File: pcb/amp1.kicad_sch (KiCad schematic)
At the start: 23 parts

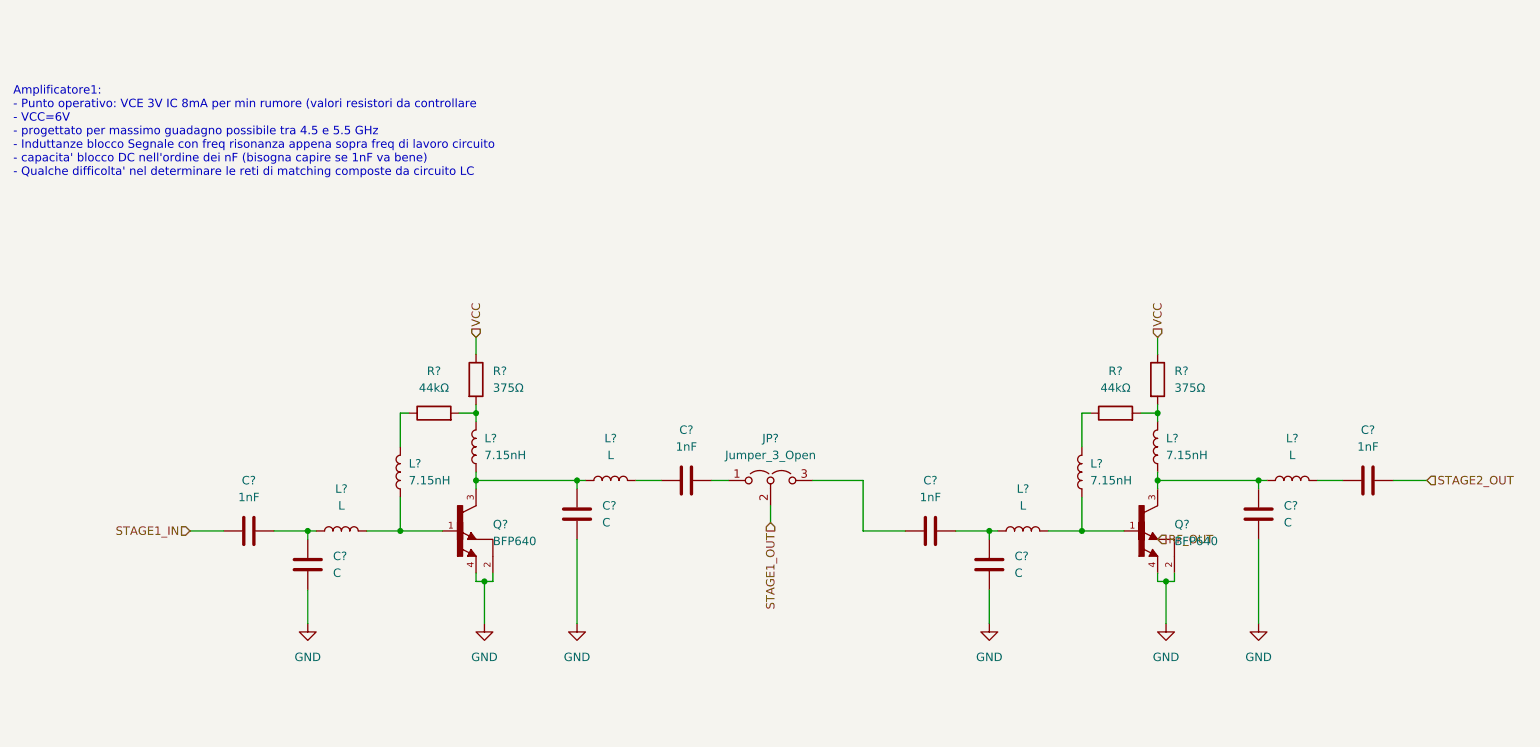
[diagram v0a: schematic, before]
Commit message: Added values for matching network
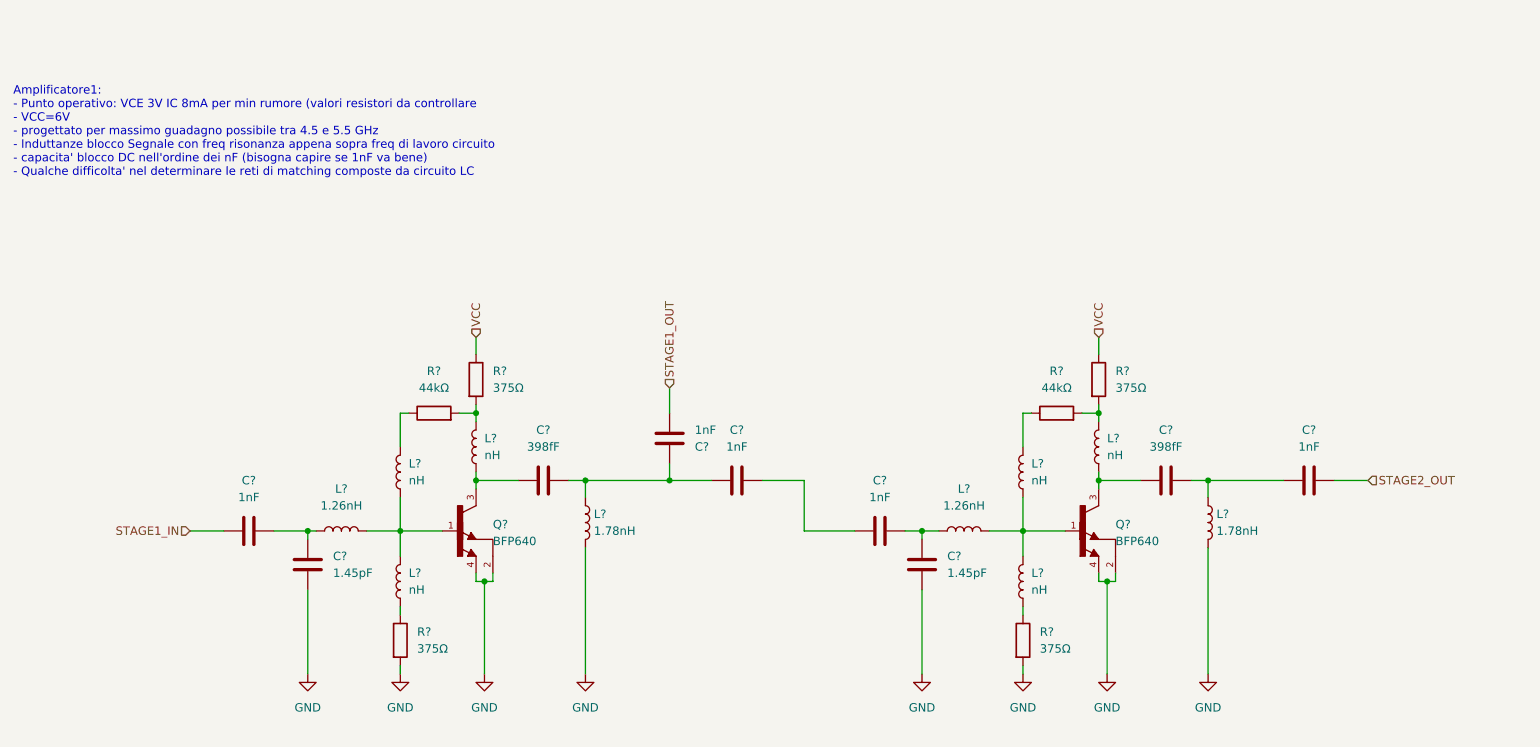
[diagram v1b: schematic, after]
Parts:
- removed C?: C, symbol Device:C
- removed JP?: Jumper_3_Open, symbol Jumper:Jumper_3_Open
- removed L?: L, symbol Device:L
- added C?: 398fF, symbol Device:C
- added C?: 1nF, symbol Device:C
- added L? (x2): nH, symbol Device:L
- added L?: 1.78nH, symbol Device:L
- added R? (x2): 375Ω, symbol Device:R
- C? (x2): value C -> 1.45pF
- C?: value C -> 398fF
- L? (x4): value 7.15nH -> nH
- L?: value L -> 1.78nH
- L? (x2): value L -> 1.26nH
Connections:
- net GND: now also L?.2, L?.2, R?.2, R?.2; no longer C?.2
- net STAGE1_OUT: now also C?.1
- net at C?.1, L?.1, Q?.3: no longer L?.1
- net at L?.1, Q?.3: now also C?.1
- net at C?.1: now also C?.2, L?.1
- net at L?.1, L?.2, Q?.1: now also L?.2 (x2)
- net at C?.2: now also C?.1
- net at C?.1: now also C?.2, L?.1, C?.2; no longer L?.2
- new net: L?.1, R?.1 (x2)
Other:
- moved on the sheet: C?, L?, Q?, R?

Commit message: Created LTSpice simulation and added suggested fix
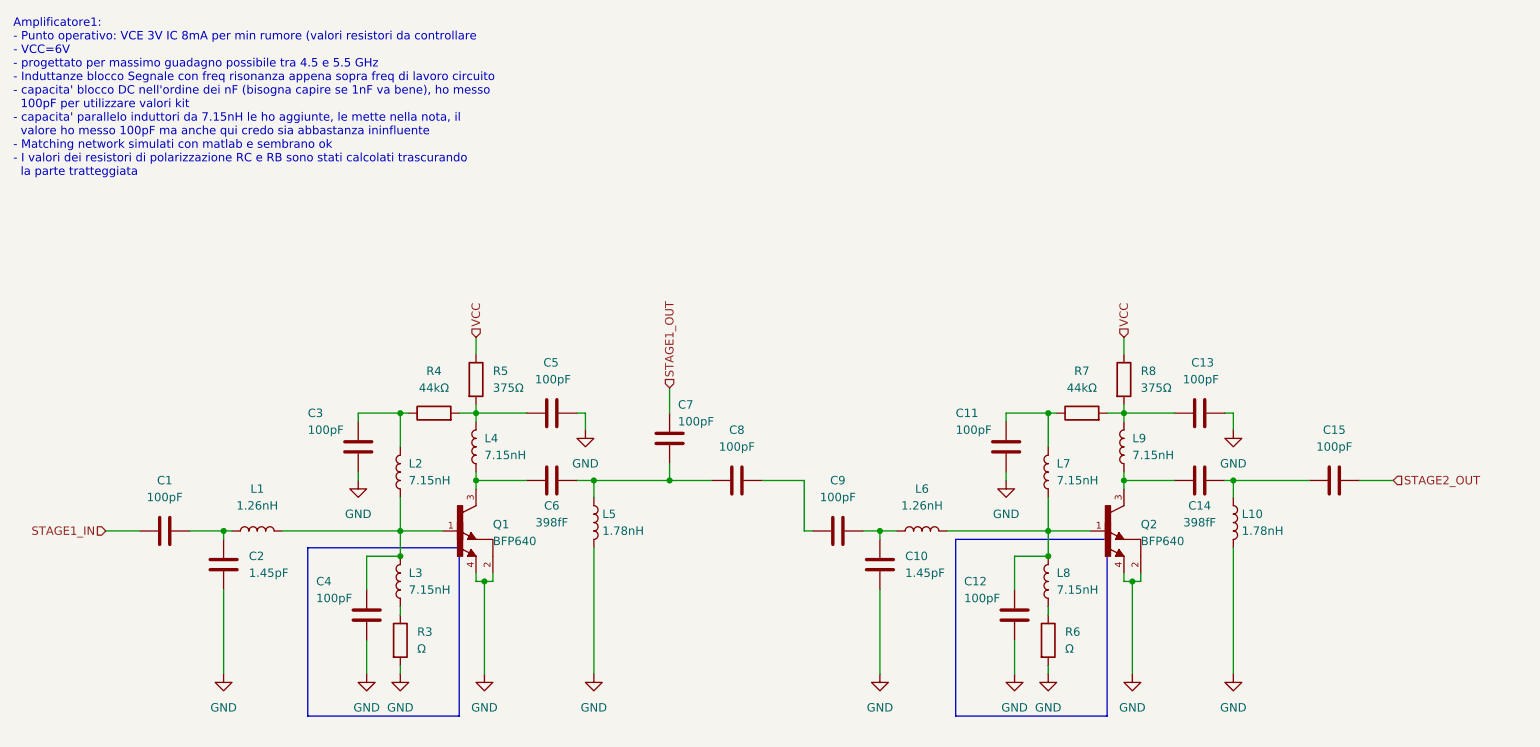
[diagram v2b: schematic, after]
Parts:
- removed L? (x6): nH, symbol Device:L
- added C11, C12, C13, C3, C4, C5: 100pF, symbol Device:C
- added L2, L3, L4, L7, L8, L9: 7.15nH, symbol Device:L
- C1, C15, C7, C8, C9: renamed from C?; value 1nF -> 100pF
- R3, R6: renamed from R?; value 375Ω -> Ω
- gave numbers to parts that had none: 14
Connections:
- net GND: now also C11.2, C12.2, C13.2, C3.2, C4.2, C5.2
- net at R3.1: now also L3.1
- net at L1.2, Q1.1: now also C4.1, L2.1, L3.2
- net at R4.2, R5.2: now also C5.1, L4.2
- net at R7.2, R8.2: now also C13.1, L9.2
- net at C14.1, Q2.3: now also L9.1
- net at C6.1, Q1.3: now also L4.1
- net at R4.1: now also C3.1, L2.2
- net at R6.1: now also L8.1
- net at R7.1: now also C11.1, L7.2
- net at L6.2, Q2.1: now also C12.1, L7.1, L8.2
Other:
- note added: "Amplificatore1: - Punto operativo: VCE 3V IC 8mA per min rumore (valori resistori da controllare - VCC=6V - progettato per massimo guadagno possibile tra 4.5 e 5.5 GHz - Induttanze blocco Segnale con freq risonanza appena sopra freq di lavoro circuito - capacita' blocco DC nell'ordine dei nF (bisogna capire se 1nF va bene), ho messo 100pF per utilizzare valori kit - capacita' parallelo induttori 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"
- note removed: "Amplificatore1: - Punto operativo: VCE 3V IC 8mA per min rumore (valori resistori da controllare - VCC=6V - progettato per massimo guadagno possibile tra 4.5 e 5.5 GHz - Induttanze blocco Segnale con freq risonanza appena sopra freq di lavoro circuito - capacita' blocco DC nell'ordine dei nF (bisogna capire se 1nF va bene) - Qualche difficolta' nel determinare le reti di matching composte da circ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"
- moved on the sheet: C1, C10, C14, C15, C2, C6, C9, L1, L10, L5, L6, Q2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

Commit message: Schematic modified as discussed
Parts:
- removed C7, C9: 100pF, symbol Device:C
- C1, C10, C11, C12, C13, C14, C15, C2, C3, C4, C5, C6, C8: footprint (none) -> Capacitor_SMD:C_0603_1608Metric
- L1, L10, L5, L6: footprint (none) -> Nicobigio01:Coilcraft_0906-xxLx
- L2, L3, L4, L7, L8, L9: footprint (none) -> Nicobigio01:Coilcraft_1606-xxLx
- R4, R5, R6, R7, R8: footprint (none) -> Resistor_SMD:R_0603_1608Metric
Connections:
- net at L6.2, L7.1, L8.2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: no longer C12.1
- net at C10.1, L6.1: now also C8.2
- net at L1.2, L2.1, L3.2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: no longer C4.1
- net at L8.1, R6.1: now also C12.1
- net at L3.1, R3.1: now also C4.1
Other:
- moved on the sheet: C12, C4, R3, R6

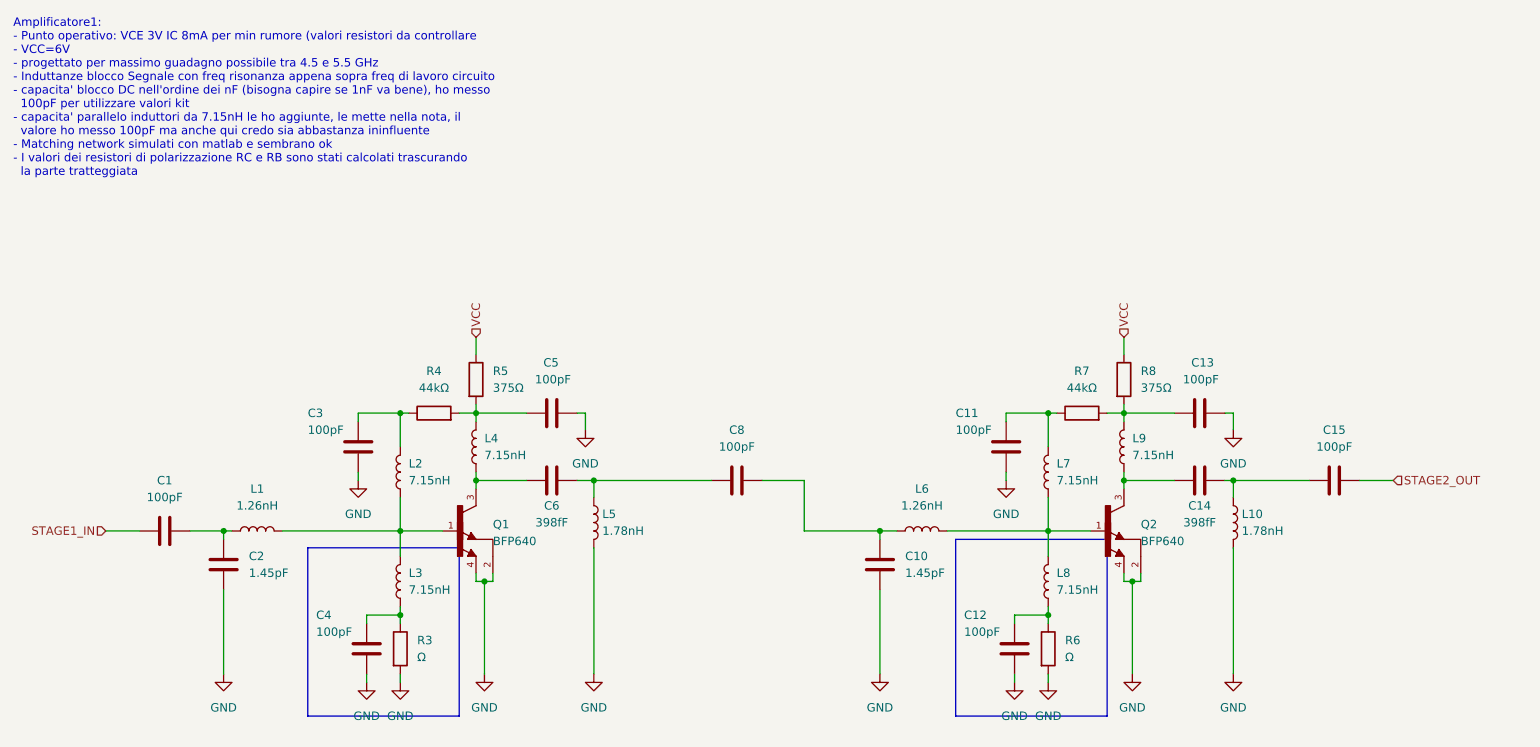
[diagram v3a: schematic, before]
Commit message: Deleted double stage, updated stub stage, L stage and PCB
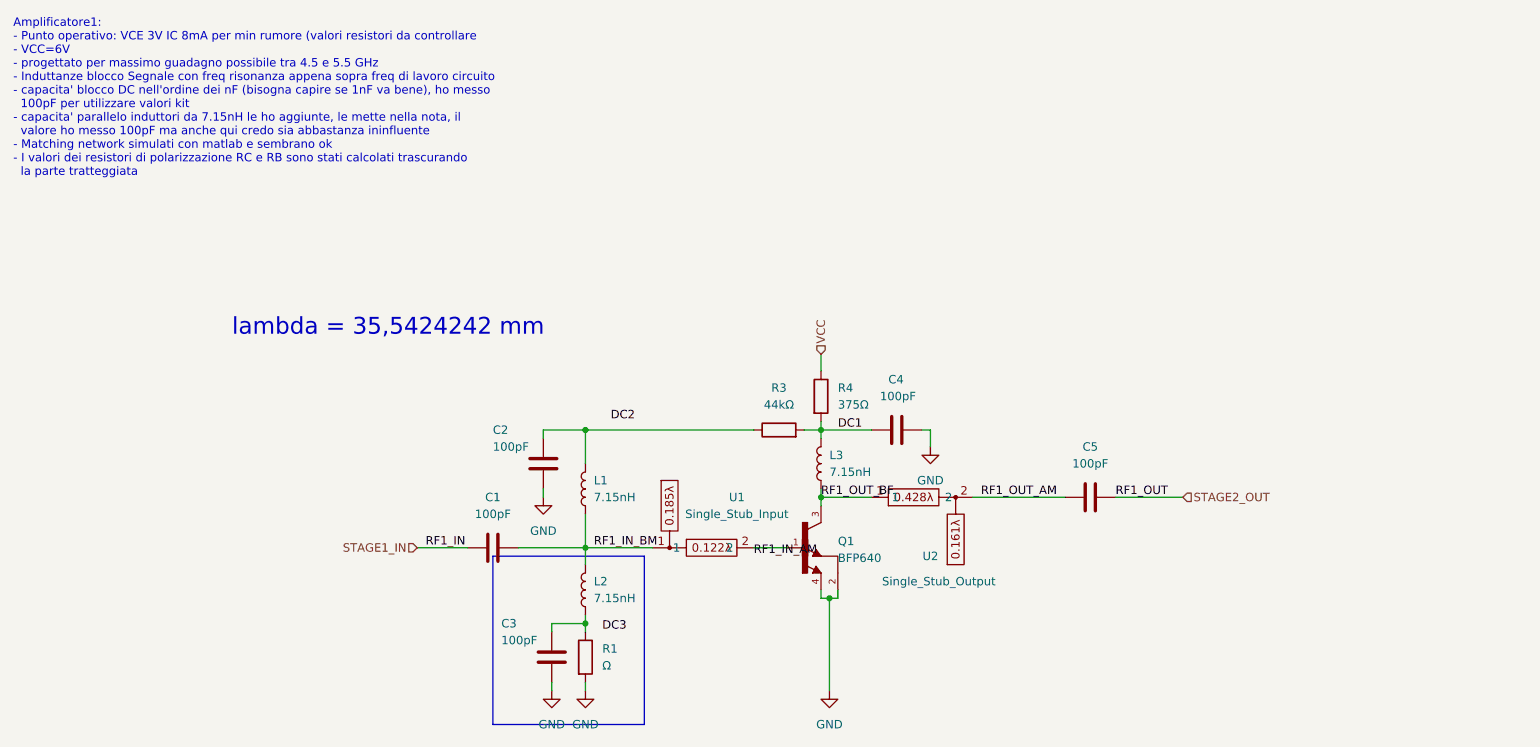
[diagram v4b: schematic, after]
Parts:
- removed C10: 1.45pF, Capacitor_SMD:C_0603_1608Metric, symbol Device:C
- removed C11, C12, C13, C15, C8: 100pF, Capacitor_SMD:C_0603_1608Metric, symbol Device:C
- removed C14, C6: 398fF, Capacitor_SMD:C_0603_1608Metric, symbol Device:C
- removed L10, L5: 1.78nH, Nicobigio01:Coilcraft_0906-xxLx, symbol Device:L
- removed L4, L7, L8, L9: 7.15nH, Nicobigio01:Coilcraft_1606-xxLx, symbol Device:L
- removed L6: 1.26nH, Nicobigio01:Coilcraft_0906-xxLx, symbol Device:L
- removed Q2: BFP640, Nicobigio01:SOT-343, symbol Nicobigio01_Transistor_HBT:BFP640
- removed R5, R8: 375Ω, Resistor_SMD:R_0603_1608Metric, symbol Device:R
- removed R6: Ω, Resistor_SMD:R_0603_1608Metric, symbol Device:R
- removed R7: 44kΩ, Resistor_SMD:R_0603_1608Metric, symbol Device:R
- added R1: Ω, Resistor_SMD:R_0603_1608Metric, symbol Device:R
- added U1: Single_Stub_Input, Nicobigio01:Microwave_Single_Stub_Input, symbol Nicobigio01_Microwave:Single_Stub_Input
- added U2: Single_Stub_Output, Nicobigio01:Microwave_SIngle_Stub_Output, symbol Nicobigio01_Microwave:Single_Stub_Output
- C2: value 1.45pF -> 100pF
- L1: value 1.26nH -> 7.15nH; footprint Nicobigio01:Coilcraft_0906-xxLx -> Nicobigio01:Coilcraft_1606-xxLx
- R3: value Ω -> 44kΩ; footprint (none) -> Resistor_SMD:R_0603_1608Metric
- R4: value 44kΩ -> 375Ω
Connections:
- net GND: now also R1.2; no longer C5.2, R3.2
- net STAGE2_OUT: now also C5.2
- net VCC: now also R4.1
- net DC1: now reaches R4.2
- net DC1: now also C4.1, L3.2, R3.2; no longer C5.1
- net RF1_OUT_BF: now reaches Q1.3
- net RF1_OUT_BF: now also L3.1, U2.1
- net RF1_IN_BM: now reaches C1.2, L1.1
- net RF1_IN_BM: now also L2.2, U1.1; no longer C2.1
- new net: C2.1, L1.2, R3.1
- new net: C3.1, L2.1, R1.1
- new net: Q1.1, U1.2
- new net RF1_OUT_AM: C5.1, U2.2
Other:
- note added: "lambda = 35,5424242 mm"
